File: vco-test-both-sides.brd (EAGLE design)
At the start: 100 x 80 mm, 25 parts, among them IC2 CEM3340

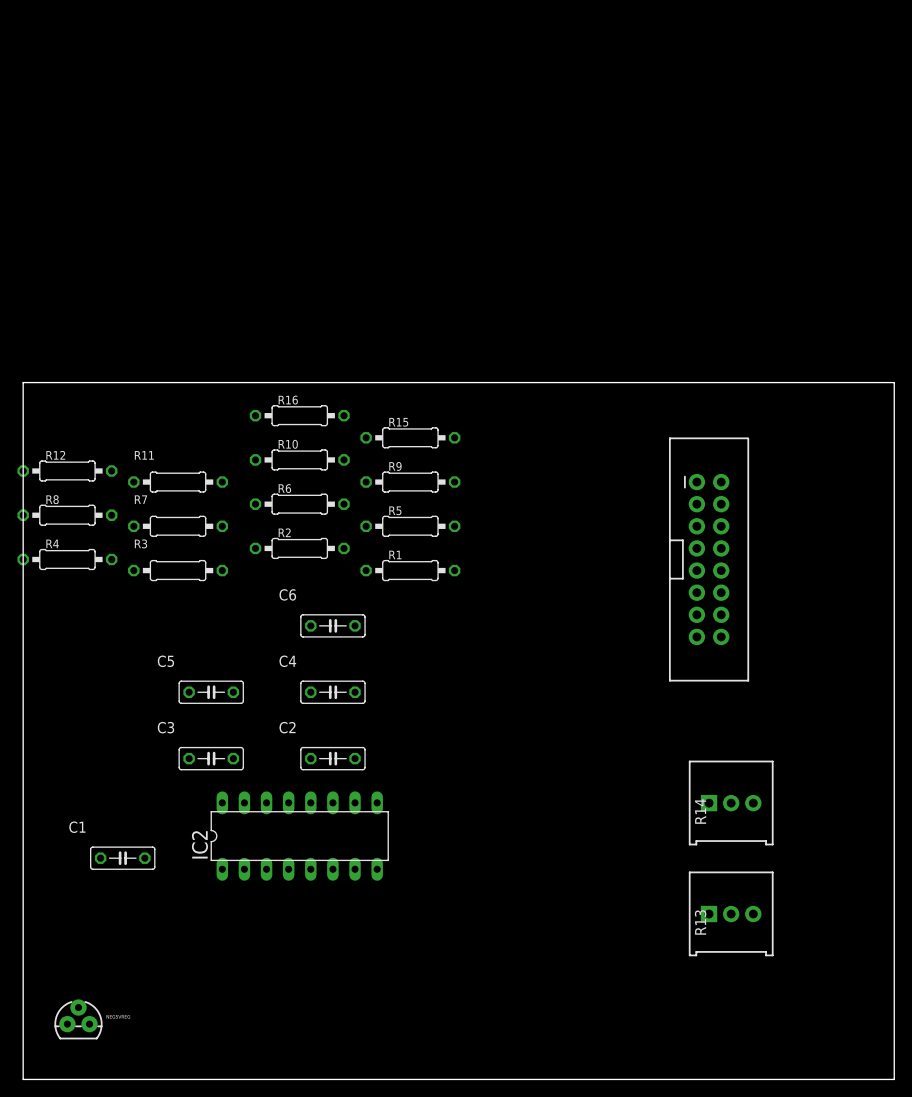
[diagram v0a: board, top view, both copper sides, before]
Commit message: Added a new project (version), using both sides of board.
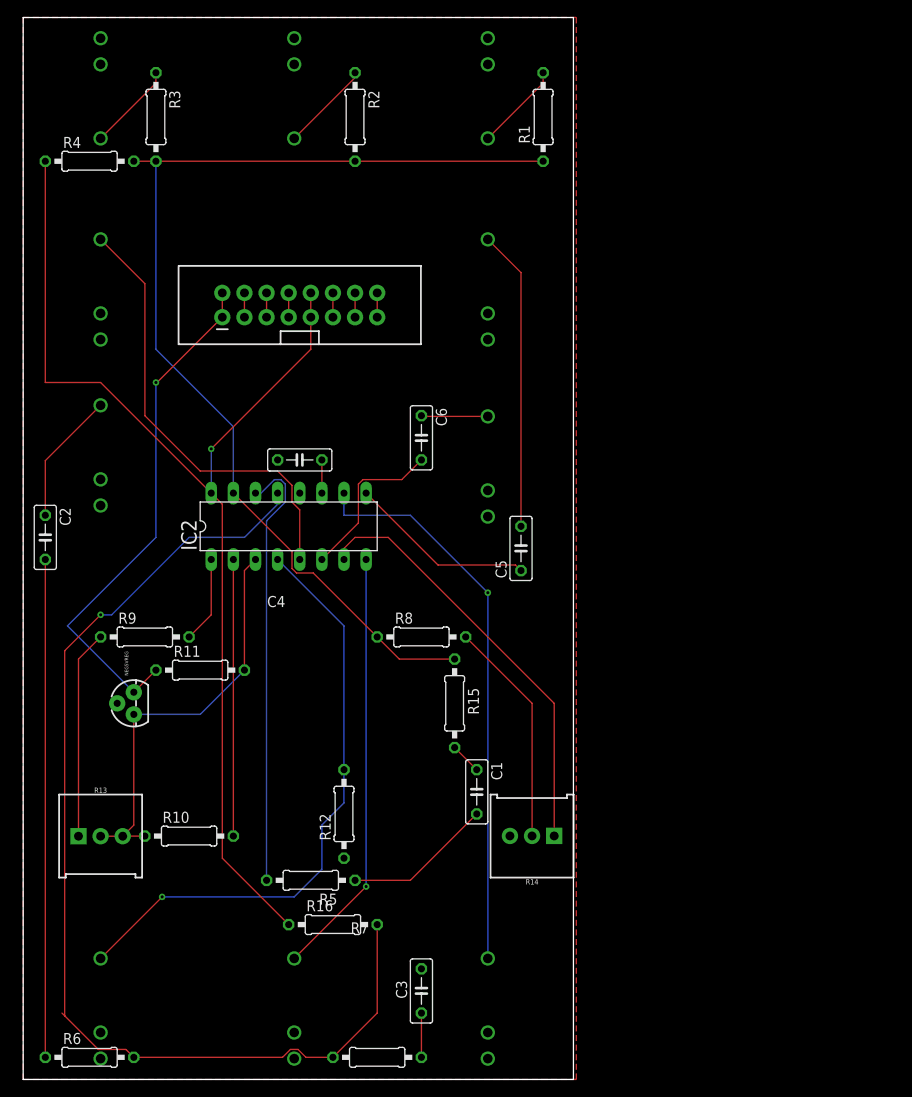
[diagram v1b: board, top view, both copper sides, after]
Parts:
- removed J1: (no value), SparkFun-Connectors:2X8-SHROUDED_LOCK
- added FREQ1, FREQ2, FREQ3, HARDSYNCIN, LINEARFMIN, PWM, SAWTOOTH, SOFTSYNC1, SQUARE, TRIANGLE: WQP-PJ301M-12_JACK, thonkiconn:WQP-PJ301M-12_JACK
- added J3: (no value), SparkFun-Connectors:2X8-SHROUDED_LOCK
- R8: value 10M -> 1M
- moved R13 72.9 mm to (8.89, 27.9)
- moved R6 67.9 mm to (7.62, 2.54)
- moved R7 65.1 mm to (40.6, 2.54)
- moved R16 58.5 mm to (35.6, 17.8)
- moved R1 54.3 mm to (59.7, 110.5), turned to 90 degrees
- moved R3 52.1 mm to (15.2, 110.5), turned to 270 degrees
- moved R12 50.6 mm to (36.8, 30.5), turned to 90 degrees
- moved R2 49.9 mm to (38.1, 110.5), turned to 270 degrees
- moved R4 45.8 mm to (7.62, 105.4)
- moved R10 45.0 mm to (19.1, 27.9)
- moved R8 43.0 mm to (45.7, 50.8)
- moved R5 42.2 mm to (33.0, 22.9), turned to 180 degrees
- moved C2 41.7 mm to (2.54, 62.2), turned to 270 degrees
- moved C1 41.3 mm to (52.1, 33.0), turned to 270 degrees
- moved C5 39.2 mm to (57.1, 61.0), turned to 90 degrees
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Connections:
- new net +5V: J3.11, J3.12
- new net CV: J3.13, J3.14
- new net GATE: J3.15, J3.16
- new net GND: C3.2, C4.2, FREQ1.P$2, FREQ1.P$3, FREQ2.P$2, FREQ2.P$3, FREQ3.P$2, FREQ3.P$3, HARDSYNCIN.P$2, HARDSYNCIN.P$3, IC2.12, J3.3, J3.4, J3.5, J3.6, J3.7, J3.8, LINEARFMIN.P$2, LINEARFMIN.P$3, NEG5VREG.2, PWM.P$2, PWM.P$3, R12.1, R14.3, SAWTOOTH.P$2, SAWTOOTH.P$3, SOFTSYNC1.P$2, SOFTSYNC1.P$3, SQUARE.P$2, SQUARE.P$3, TRIANGLE.P$2, TRIANGLE.P$3
- new net N$14: FREQ1.P$1, R1.2
- new net N$16: C6.1, HARDSYNCIN.P$1
- new net N$20: FREQ2.P$1, R2.1
- new net N$22: FREQ3.P$1, R3.1
- new net N$23: IC2.10, TRIANGLE.P$1
- new net N$24: C2.1, LINEARFMIN.P$1
- new net N$29: C5.2, SOFTSYNC1.P$1
- new net N$31: IC2.8, SAWTOOTH.P$1
- new net N$35: IC2.5, PWM.P$1
- net +12V: now also J3.10, J3.9, R4.1
- net -12V: now also J3.1, J3.2; no longer R10.1, R13.2, R13.3
- net N$12: now also R10.1, R13.2, R13.3
- net N$18: now also SQUARE.P$1
- net PE: no longer C3.2, C4.2, IC2.12, NEG5VREG.2, R12.1, R14.3
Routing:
- net +12V: track 0.00 -> 131.2 mm, vias 0 -> 1
- net N$4: track 0.00 -> 125.9 mm, vias 0 -> 1
- net N$21: track 0.00 -> 124.5 mm
- net N$18: track 0.00 -> 69.4 mm, vias 0 -> 1
- net N$23: track 0.00 -> 64.7 mm, vias 0 -> 1
- net -12V: track 0.00 -> 60.0 mm, vias 0 -> 1
- net N$5: track 0.00 -> 57.1 mm
- net N$35: track 0.00 -> 51.5 mm
- net N$3: track 0.00 -> 50.7 mm
- net N$31: track 0.00 -> 49.2 mm, vias 0 -> 1
- net N$13: track 0.00 -> 49.0 mm
- net N$12: track 0.00 -> 47.6 mm
- net N$29: track 0.00 -> 34.5 mm
- net N$1: track 0.00 -> 31.7 mm
- net N$10: track 0.00 -> 26.0 mm
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- added copper zone on layer 1, net GND
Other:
- board size 100 x 80 mm -> 63.2 x 121.9 mm
